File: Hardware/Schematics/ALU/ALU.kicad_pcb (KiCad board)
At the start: 4 copper layers, 188.4 x 135.2 mm, 54 parts, among them J1 Conn_01x10, J2 Conn_01x10, J3 Conn_02x05_Counter_Clockwise, J4 Conn_01x10, J5 Conn_02x05_Counter_Clockwise, U1 74LS113, U10 74LS83, U11 74LS83, U12 74LS245, U13 74LS00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

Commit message: Updated Schematics
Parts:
- removed REF** (x4): MountingHole_5.3mm_M5, MountingHole:MountingHole_5.3mm_M5
- moved C16 113.4 mm to (89.0, 30.5)
- moved C4 80.5 mm to (137.4, 103.2)
- moved U7 80.5 mm to (130.2, 84.4)
- moved U21 79.9 mm to (130.2, 63.4)
- moved C5 79.9 mm to (137.7, 60.0)
- moved U20 77.9 mm to (106.4, 119.2), turned to 90 degrees
- moved C2 73.4 mm to (126.0, 60.3)
- moved U19 73.4 mm to (118.7, 63.3)
- moved C10 71.4 mm to (125.6, 111.7), turned to -90 degrees
- moved U16 69.5 mm to (94.1, 47.1)
- moved J5 69.3 mm to (72.2, 25.0)
- moved U18 60.7 mm to (129.2, 48.4)
- moved U17 57.0 mm to (107.6, 82.2)
- moved RN1 56.8 mm to (119.4, 108.1)
- moved C13 53.2 mm to (113.5, 22.7)
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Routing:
- net VCC: track 992.1 -> 627.8 mm, vias 2 -> 0
- net /Compare/RD != RS: track 498.7 -> 165.7 mm, vias 2 -> 3
- net /Adder/RD_{0}: track 421.9 -> 118.0 mm
- net /Adder/RD_{1}: track 408.0 -> 125.4 mm, vias 0 -> 3
- net /Adder/RD_{2}: track 383.9 -> 107.3 mm, vias 0 -> 4
- net GND: track 393.6 -> 666.3 mm, vias 1 -> 0
- net /Adder/RD_{3}: track 374.0 -> 103.4 mm, vias 0 -> 2
- net /Adder/RD_{5}: track 408.2 -> 148.7 mm
- net /Adder/RD_{4}: track 396.1 -> 149.7 mm, vias 0 -> 1
- net /Adder/RD_{6}: track 368.6 -> 128.2 mm, vias 0 -> 1
- net /Adder/RD_{7}: track 358.1 -> 122.9 mm, vias 0 -> 2
- net /Compare/RD == RS: track 269.6 -> 113.2 mm, vias 0 -> 3
- net /Adder/RS_{4}: track 253.7 -> 106.8 mm
- net /Adder/RS_{7}: track 255.5 -> 119.3 mm, vias 0 -> 3
- net /Adder/RS_{1}: track 251.5 -> 115.7 mm, vias 0 -> 1
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- removed copper zone on B.Cu, net GND
- removed copper zone on F.Cu, net GND
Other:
- board size 188.4 x 135.2 mm -> 101.8 x 101.1 mm
- copper layers 4 -> 2

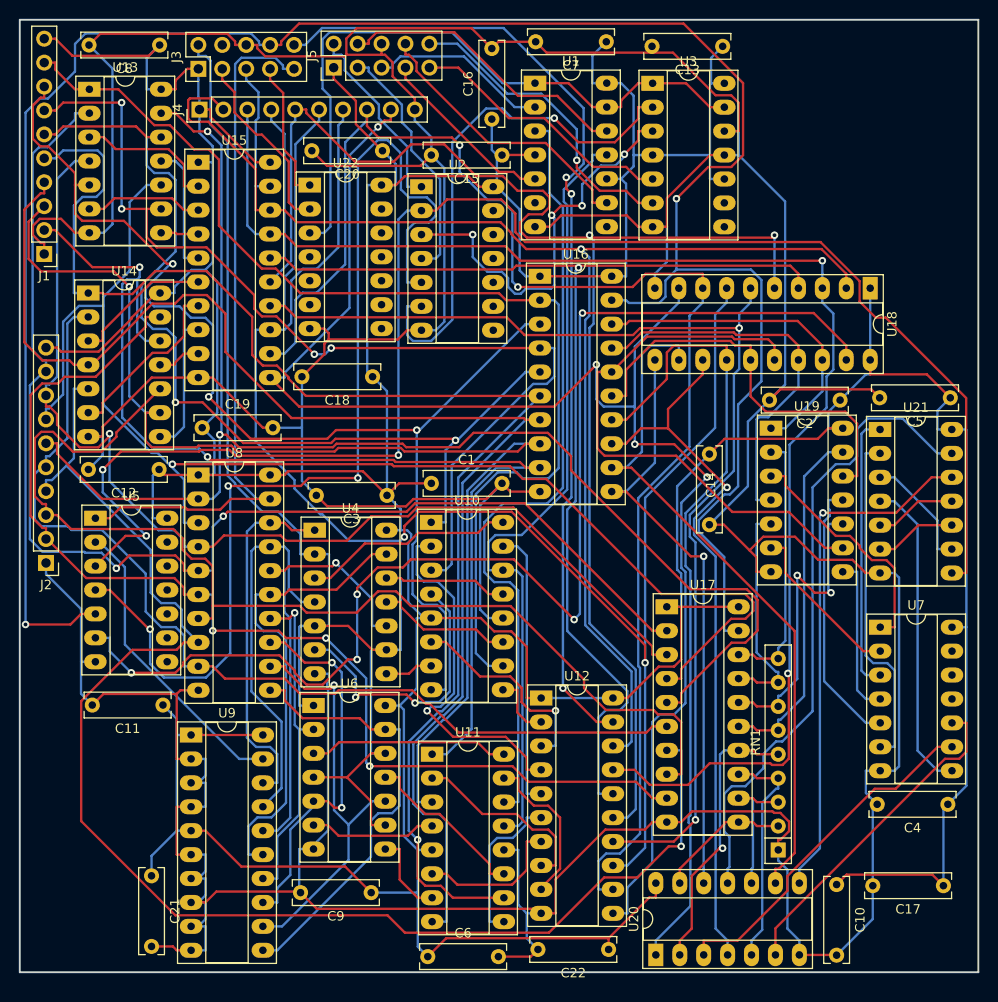
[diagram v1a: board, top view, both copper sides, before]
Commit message: Updated and Created more Schems
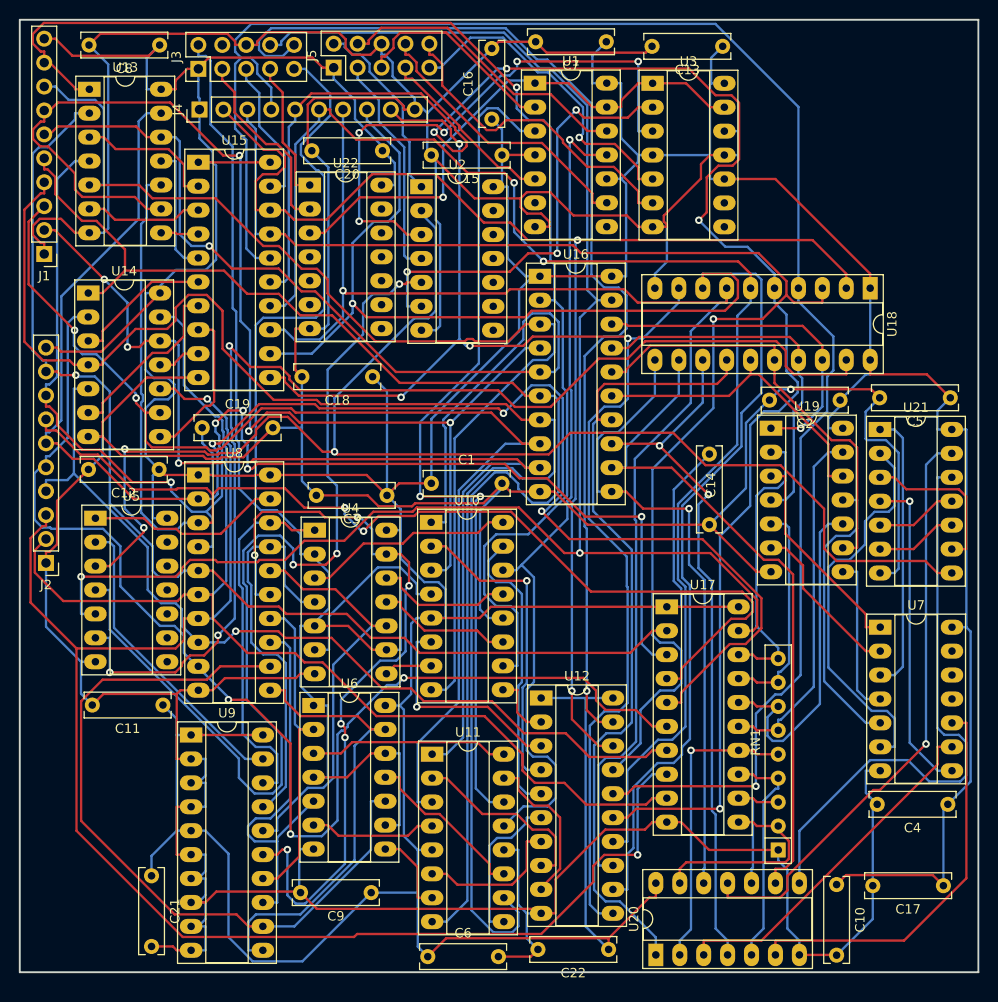
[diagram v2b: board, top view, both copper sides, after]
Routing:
- net /Compare/~{CMP}: track 234.2 -> 177.6 mm
- net /Adder/RS_{5}: track 151.3 -> 95.3 mm
- net VCC: track 627.8 -> 680.4 mm
- net /Adder/Out_{2}: track 139.4 -> 190.7 mm
- net /Adder/RS_{6}: track 118.4 -> 163.7 mm, vias 0 -> 2
- net Net-(U6-Pad10): track 44.2 -> 79.8 mm, vias 1 -> 0
- net Net-(U4-Pad13): track 49.6 -> 82.1 mm, vias 0 -> 6
- net /Adder/Out_{3}: track 157.2 -> 182.6 mm, vias 2 -> 4
- net /Adder/RS_{4}: track 106.8 -> 131.3 mm, vias 0 -> 3
- net /Adder/RS_{1}: track 115.7 -> 138.9 mm, vias 1 -> 5
- net /Adder/RD_{0}: track 118.0 -> 140.3 mm, vias 0 -> 1
- net /Adder/Out_{5}: track 164.9 -> 144.2 mm, vias 2 -> 1
- net /Adder/RD_{2}: track 107.3 -> 127.7 mm, vias 4 -> 3
- net /Compare/RD != RS: track 165.7 -> 149.1 mm
- net Net-(U2-Pad3): track 43.0 -> 59.3 mm, vias 4 -> 5
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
